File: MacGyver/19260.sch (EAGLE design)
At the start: 127 parts, among them J1 PST1,0/2-3,5, J10 RJ45J, J13 S04B, J2 PPPC101LFBN, J3 PPPC101LFBN, J4 PPPC101LFBN, J7 Pi Zero, J8 PST1,0/3-3,5, J9 RJ45J, Q1 IRFR5305, Q10 K38, Q11 K38, Q2 K1N, Q201 K1N, Q202 K1N, Q203 K1N, Q3 IRFR5305, Q4 P65, Q5 K3N, Q6 K1N, Q7 K3N, Q8 P65, Q9 K38, U1 1087, U2 1087, U201 74LVC07A, U202 74LVC07A, U203 THVD1500, U204 THVD1500, U205 THVD1500, U206 ATMEGA328PB-AU, U3 I50115, U4 I50115, U5 AVR128DA28-I/SP, Y201 12MHz

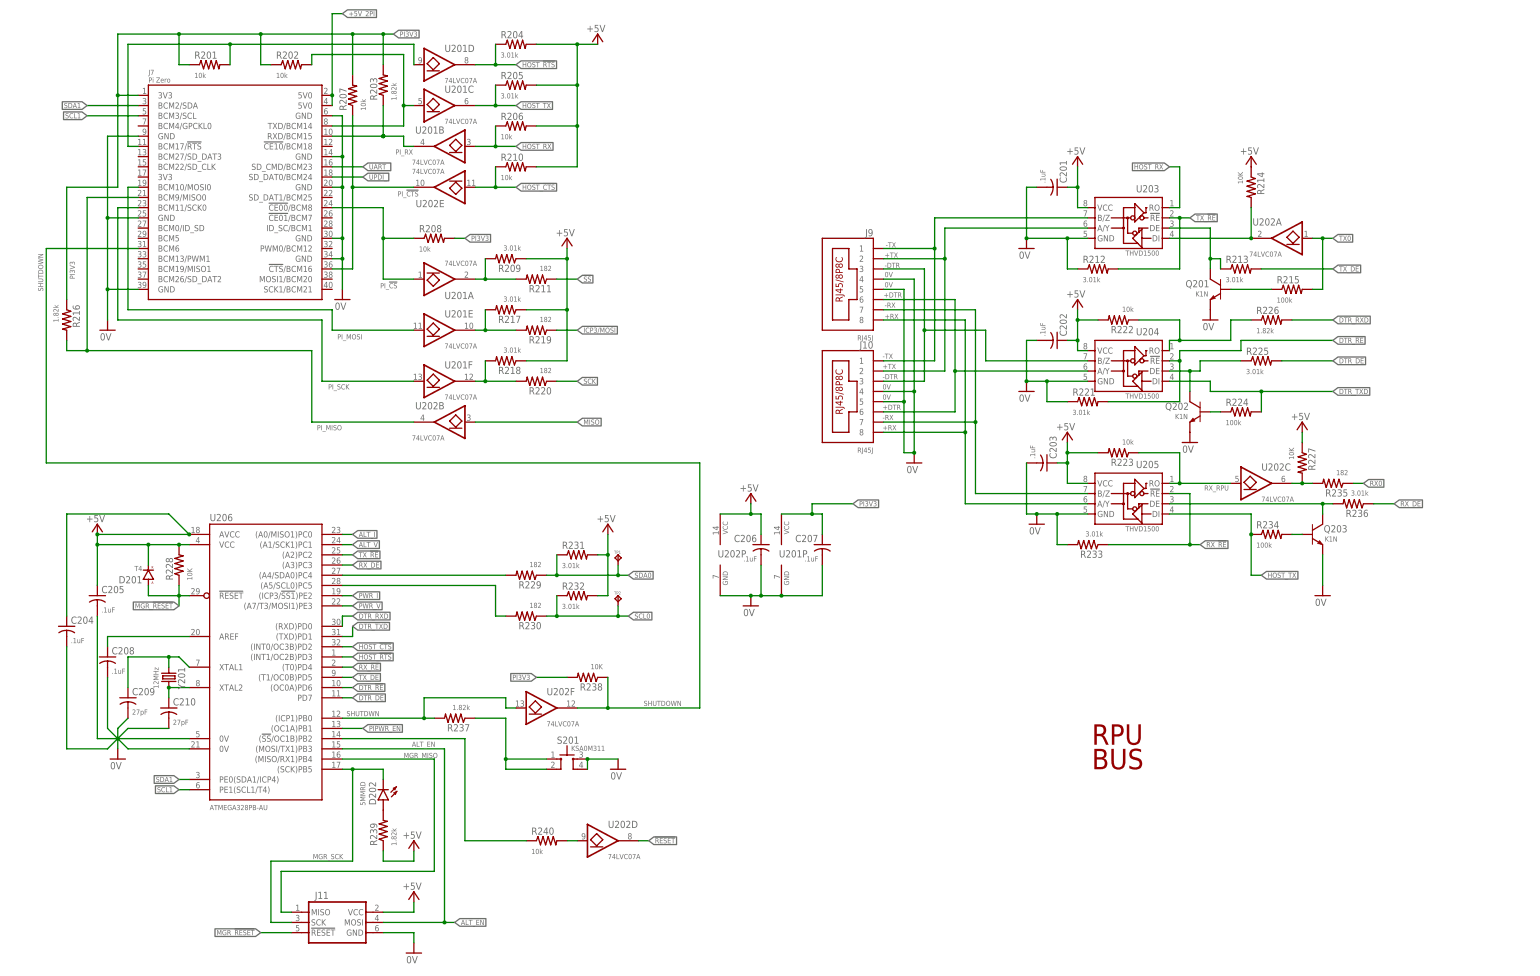
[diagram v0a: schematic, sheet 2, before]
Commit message: MacGyger: manager will be avr-db, remove spi
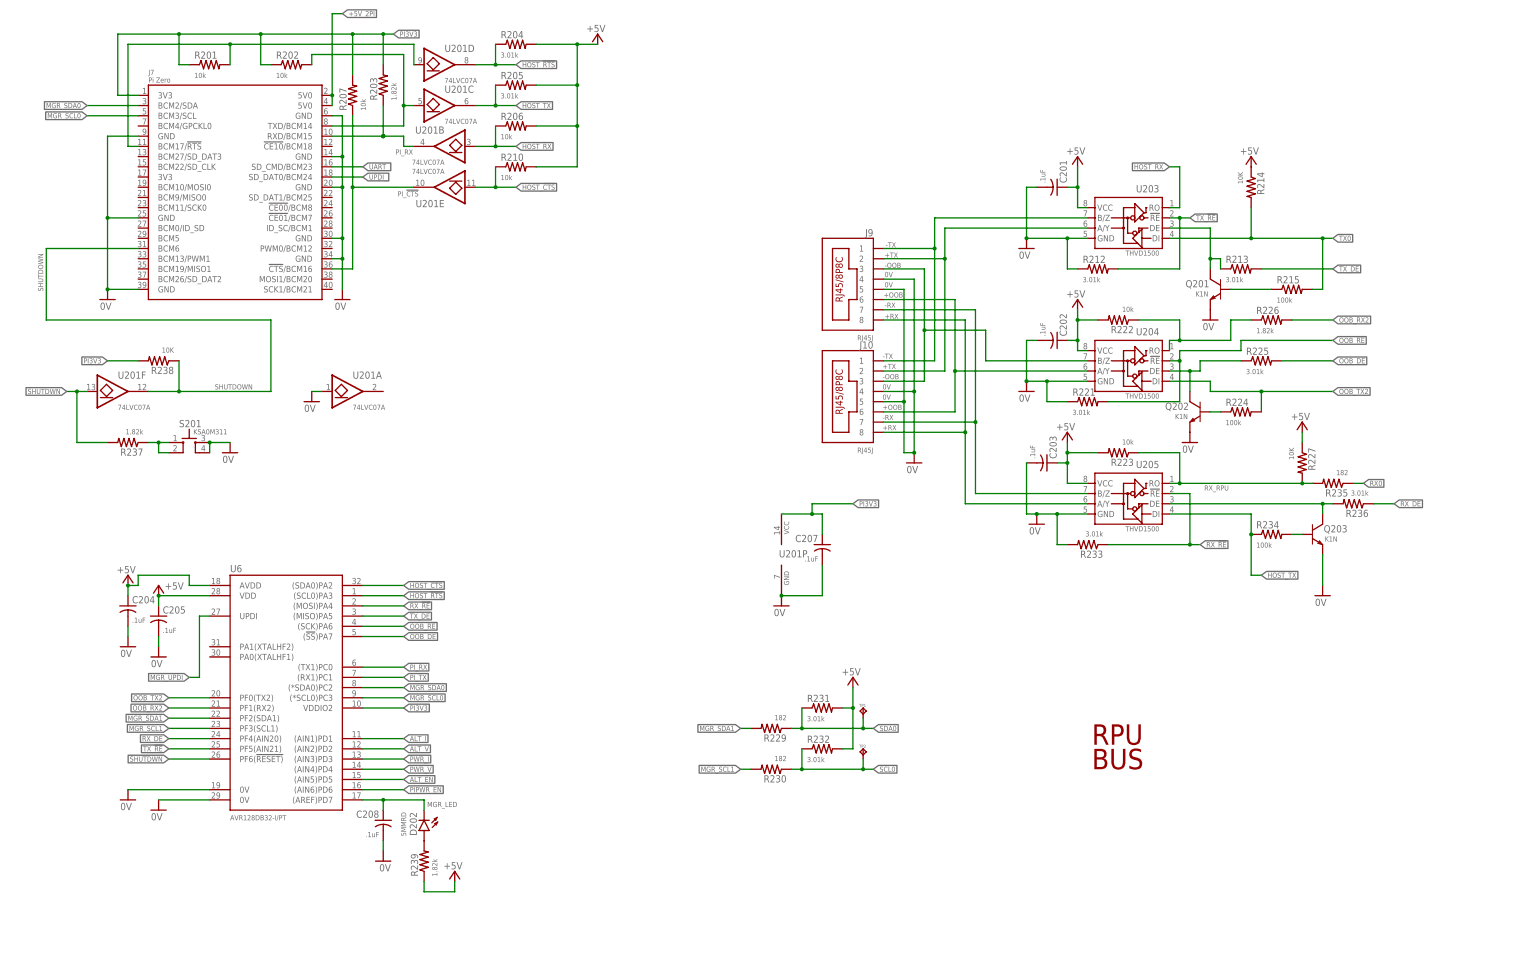
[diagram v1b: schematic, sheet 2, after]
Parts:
- removed C206: .1uF, C-C:CC0603A
- removed C209, C210: 27pF, C-C:CC0603A
- removed D201: T4, D-GP:DSOD123
- removed J11: (no value), U-AVR:ISP-SPIPTH
- removed R208, R240: 10k, R-C:R0805
- removed R209, R217, R218: 3.01k, R-C:R0805
- removed R211, R219, R220: 182, R-C:R0805
- removed R216: 1.82k, R-C:R0805
- removed R228: 10K, R-C:R0805
- removed U202: 74LVC07A, U-7400:7407D
- removed U206: ATMEGA328PB-AU, U-AVR:ATMEGA328PB-AU
- removed Y201: 12MHz, Y-XTL:CSM-3X
- added U6: AVR128DB32-I/PT, U-AVR:AVR128DB32
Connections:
- net +DTR renamed +OOB
- net -DTR renamed -OOB
- removed net !RESET!: U202D.O
- removed net DTR_!RE: R221.2, U204.!RE, U206.(OC0A)PD6
- removed net DTR_DE: R225.2, U206.PD7
- removed net DTR_RXD: R226.2, U206.(RXD)PD0
- removed net DTR_TXD: R224.2, U204.DI, U206.(TXD)PD1
- removed net ICP3/MOSI: R219.1
- removed net MGR_!RESET: D201.A, J11.!RESET, R228.1, U206.!RESET
- removed net MGR_!SS!: R240.1, U206.(!SS!/OC1B)PB2
- removed net MGR_AREF: C208.1, U206.AREF
- removed net MGR_MISO: J11.MISO, U206.(MISO/RX1)PB4
- removed net MGR_SCK: D202.K, J11.SCK, U206.(SCK)PB5
- removed net N$78: R227.2, R235.2, U202C.O
- removed net N$88: R240.2, U202D.I
- removed net N$91: R218.2, R220.2, U201F.O
- removed net N$92: R217.2, R219.2, U201E.O
- removed net N$94: R229.2, U206.(A4/SDA0)PC4
- removed net N$95: R230.2, U206.(A5/SCL0)PC5
- removed net N$96: R209.2, R211.2, U201A.O
- removed net PI_!CS: J7.!CE00!/BCM8, R208.1, U201A.I
- removed net PI_MISO: J7.BCM9/MISO0, R216.2, U202B.O
- removed net PI_MOSI: J7.BCM10/MOSI0, U201E.I
- removed net PI_SCK: J7.BCM11/SCK0, U201F.I
- removed net SCL1: J7.BCM3/SCL, U206.PE1(SCL1/T4)
- removed net SDA1: J7.BCM2/SDA, U206.PE0(SDA1/ICP4)
- removed net TX_RPU: R214.2, U202A.O, U203.DI
- removed net XTAL1: C209.1, U206.XTAL1, Y201.1
- removed net XTAL2: C210.1, U206.XTAL2, Y201.2
- new net MGR_LED: C208.1, D202.K, U6.(AREF)PD7
- new net MGR_SCL0: J7.BCM3/SCL, U6.(*SCL0)PC3
- new net MGR_SCL1: R230.2, U6.PF3(SCL1)
- new net MGR_SDA0: J7.BCM2/SDA, U6.(*SDA0)PC2
- new net MGR_SDA1: R229.2, U6.PF2(SDA1)
- new net MGR_UPDI: U6.UPDI
- new net OOB_!RE: R221.2, U204.!RE, U6.(SCK)PA6
- new net OOB_DE: R225.2, U6.(!SS!)PA7
- new net OOB_RX2: R226.2, U6.PF1(RX2)
- new net OOB_TX2: R224.2, U204.DI, U6.PF0(TX2)
- new net PI_TX: U6.(RX1)PC1
- net !SS: no longer R211.1
- net +5V: now also U6.AVDD, U6.VDD; no longer C206.1, D201.K, J11.VCC, R209.1, R217.1, R218.1, R228.2, U202P.VCC, U206.AVCC, U206.VCC@0
- net 0V: now also U201A.I, U6.0V@0, U6.0V@1; no longer C206.2, C209.2, C210.2, J11.GND, U202P.GND, U206.0V@0, U206.0V@1
- net ALT_EN: now also U6.(AIN5)PD5; no longer J11.MOSI, U206.(MOSI/TX1)PB3
- net ALT_I: now also U6.(AIN1)PD1; no longer U206.(A0/MISO1)PC0
- net ALT_V: now also U6.(AIN2)PD2; no longer U206.(A1/SCK1)PC1
- net HOST_!CTS: now also U201E.I, U6.(SDA0)PA2; no longer U202E.I, U206.(INT0/OC3B)PD2
- net HOST_!RTS: now also U6.(SCL0)PA3; no longer U206.(INT1/OC2B)PD3
- net MISO: no longer U202B.I
- net PI3V3: now also U6.VDDIO2; no longer R208.2, R216.1
- net PIPWR_EN: now also U6.(AIN6)PD6; no longer U206.(OC1A)PB1
- net PI_!CTS: now also U201E.O; no longer U202E.O
- net PI_RX: now also U6.(TX1)PC0
- net PWR_I: now also U6.(AIN3)PD3; no longer U206.(ICP3/!SS1!)PE2
- net PWR_V: now also U6.(AIN4)PD4; no longer U206.(A7/T3/MOSI1)PE3
- net RX_!RE: now also U6.(MOSI)PA4; no longer U206.(T0)PD4
- net RX_DE: now also U6.PF4(AIN20); no longer U206.(A3)PC3
- net RX_RPU: now also R227.2, R235.2; no longer U202C.I
- net SCK: no longer R220.1
- net SHUTDOWN: now also U201F.O; no longer U202F.O
- net SHUTDWN: now also U201F.I, U6.PF6(!RESET); no longer U202F.I, U206.(ICP1)PB0
- net TX0: now also R214.2, U203.DI; no longer U202A.I
- net TX_!RE: now also U6.PF5(AIN21); no longer U206.(A2)PC2
- net TX_DE: now also U6.(MISO)PA5; no longer U206.(T1/OC0B)PD5
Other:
- note added: "1"
- note added: "15"
- note added: "17"
- note added: "2"
- note added: "25"
- note added: "32"
- note added: "BUS MANAGER NEEDS TO DRIVE OOB_DE BUT A HIGH OOB_TX OVERIDES"
- note added: "I2C to APP"
- note added: "IF AREF NEEDS BYPASS"
- note added: "MVIO"
- note added: "OOB"
- note added: "OUT OF BAND"
- note added: "SMBus to Pi"
- note added: "debug"
- note removed: "BUS MANAGER NEEDS TO DRIVE DTR_DE BUT A HIGH DTR_TXD OVERIDES"
- note removed: "CNTL RESET"
- note removed: "CRYSTAL: ECS-120-20-3X-TR 12MHZ +/- 30PPM STABILITY AND TOLERANCE CRYSTAL CAPACITORS: 20PF = 6.5PF + (27PF*27PF)/(27PF+27PF)"
- note removed: "DTR"
- note removed: "MGR ICSP"
- note removed: "REMOVE ALTERNAT POWER BEFOR ISP PROGRAMING"
- moved on the sheet: C204, C205, C208, D202, R229, R230, R231, R232, R237, R238, R239, S201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

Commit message: MacGyver: remove rts/cts since no bootloader
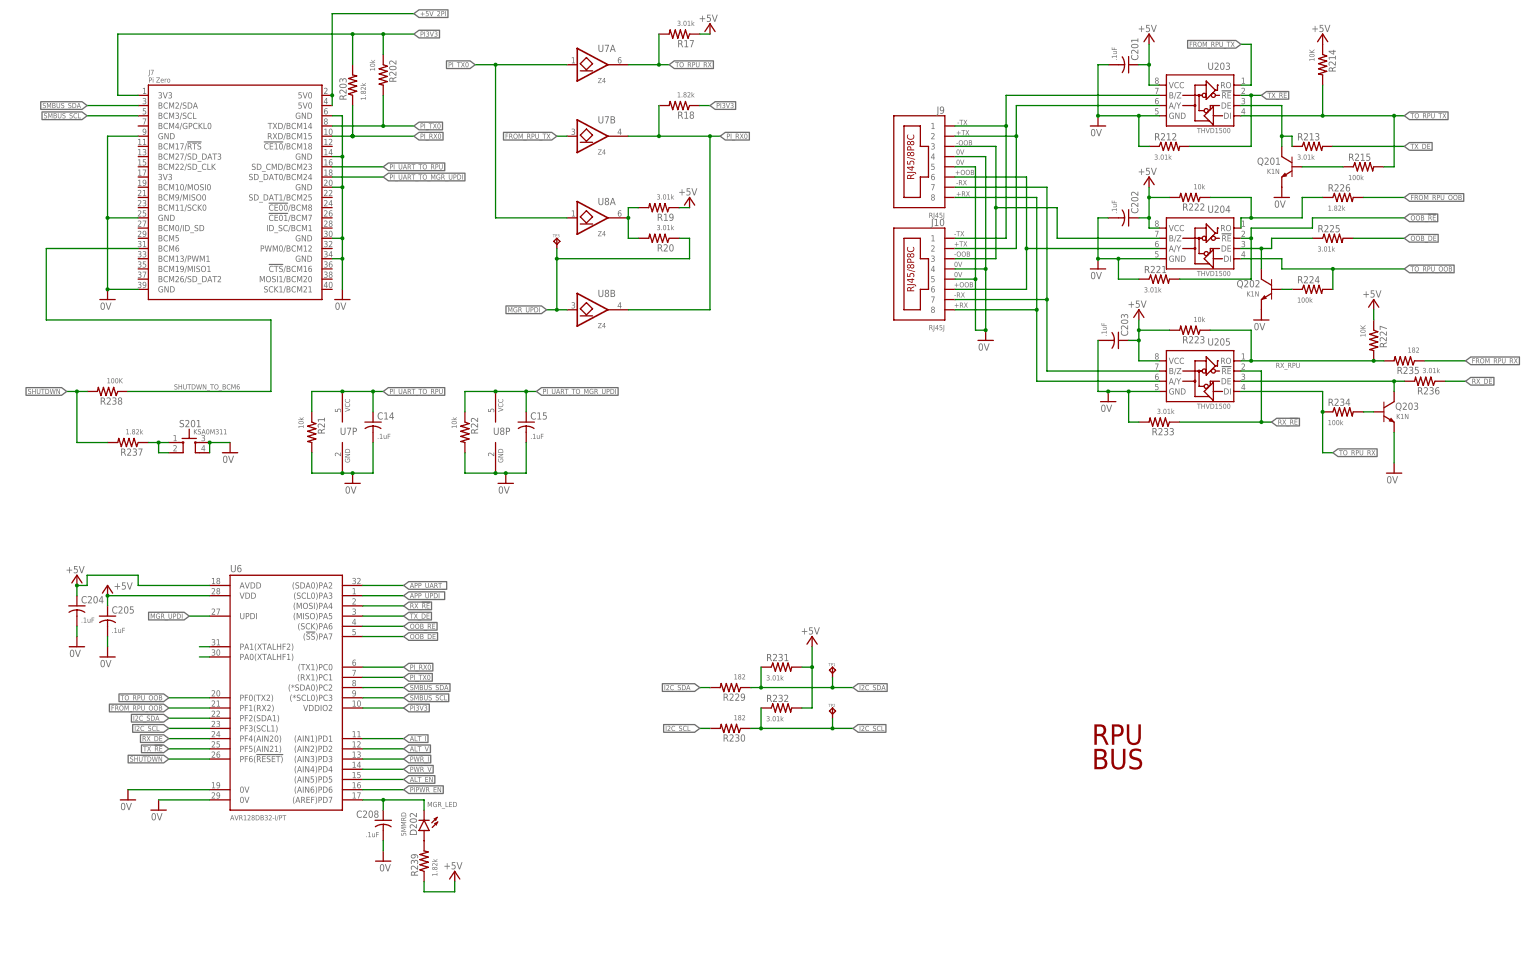
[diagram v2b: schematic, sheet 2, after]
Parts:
- removed C207: .1uF, C-C:CC0603A
- removed R201, R206, R207, R210: 10k, R-C:R0805
- removed R204, R205: 3.01k, R-C:R0805
- removed U201: 74LVC07A, U-7400:7407D
- added C14, C15, C16, C17: .1uF, C-C:CC0603A
- added R17, R19, R20, R23, R24, R25, R26: 3.01k, R-C:R0805
- added R18: 1.82k, R-C:R0805
- added R21, R22, R27, R28: 10k, R-C:R0805
- added TP3: TPPAD1-08, J-TP:TPPAD1-08
- added U10, U7, U8, U9: Z4, U-7400:2G07SOT26
- R238: value 10K -> 100K
- R3: value 0.018 -> 0.010
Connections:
- net MGR_SCL0 renamed SMBUS_SCL
- net MGR_SCL1 renamed I2C_SCL_
- net MGR_SDA0 renamed SMBUS_SDA
- net MGR_SDA1 renamed I2C_SDA_
- net OOB_RX2 renamed FROM_RPU_OOB
- net OOB_TX2 renamed TO_RPU_OOB
- net SCL0 renamed I2C_SCL
- net SDA0 renamed I2C_SDA
- removed net HOST_!CTS: R210.1, U201E.I, U6.(SDA0)PA2
- removed net HOST_!RTS: R204.1, U201D.O, U6.(SCL0)PA3
- removed net HOST_RX: R206.1, U201B.I, U203.RO
- removed net HOST_TX: R205.1, R234.1, U201C.O, U205.DI
- removed net N$89: J7.TXD/BCM14, R202.2, U201C.I
- removed net N$90: J7.BCM17/!RTS!, R201.2, U201D.I
- removed net PI_!CTS: J7.!CTS!/BCM16, R207.1, U201E.O
- removed net PI_RX: J7.RXD/BCM15, R203.1, U201B.O, U6.(TX1)PC0
- removed net PI_TX: U6.(RX1)PC1
- removed net RX0: J4.7, R235.1, U5.(RX0)PA1
- removed net SHUTDOWN: J7.BCM6, R238.1, U201F.O
- removed net TX0: J4.6, R214.2, R215.2, U203.DI, U5.(EXTCLK/TX0)PA0
- removed net UART_: J7.SD_CMD/BCM23
- removed net UPDI_: J7.SD_DAT0/BCM24
- new net APP_RX0: J4.7, R23.2, U5.(RX0)PA1, U9A.O
- new net APP_TX0: J4.6, U5.(EXTCLK/TX0)PA0, U9B.I
- new net APP_UART_: C16.1, R27.1, U6.(SDA0)PA2, U9P.VCC
- new net APP_UPDI_: C17.1, R28.1, U10P.VCC, U6.(SCL0)PA3
- new net FROM_RPU_RX: R235.1, U10A.I, U9A.I
- new net FROM_RPU_TX: U203.RO, U7B.I
- new net N$1: R19.2, R20.2, U8A.O
- new net N$11: U6.PA0(XTALHF1)
- new net N$3: R25.2, R26.2, U10A.O
- new net N$9: U6.PA1(XTALHF2)
- new net PI_RX0: J7.RXD/BCM15, R18.2, R203.1, U6.(TX1)PC0, U7B.O, U8B.O
- new net PI_TX0: J7.TXD/BCM14, R202.2, U6.(RX1)PC1, U7A.I, U8A.I
- new net PI_UART_TO_MGR_UPDI: C15.1, J7.SD_DAT0/BCM24, R22.1, U8P.VCC
- new net PI_UART_TO_RPU: C14.1, J7.SD_CMD/BCM23, R21.1, U7P.VCC
- new net SHUTDWN_TO_BCM6: J7.BCM6, R238.1
- new net TO_RPU_RX: R17.2, R234.1, U205.DI, U7A.O
- new net TO_RPU_TX: R214.2, R215.2, R24.2, U10B.O, U203.DI, U9B.O
- net +5V: now also R17.1, R19.1, R23.1, R24.1, R25.1; no longer R204.2, R205.2, R206.2, R210.2
- net 0V: now also C14.2, C15.2, C16.2, C17.2, R21.2, R22.2, R27.2, R28.2, U10P.GND, U7P.GND, U8P.GND, U9P.GND; no longer C207.2, U201A.I, U201P.GND
- net MGR_UPDI: now also R20.1, TP3.TP, U8B.I
- net PI3V3: now also R18.1; no longer C207.1, R201.1, R207.2, R238.2, U201P.VCC
- net SHUTDWN: now also R238.2; no longer U201F.I
- net UPDI-APP: now also R26.1, U10B.I
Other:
- note added: "DRIVE SIDE DOES NOT NEED PULL-UP"
- note added: "ENABLE NORMAL FULL DUPLEX SERIAL FROM RPU TO APPLICATION ON ITS UART0"
- note added: "ENABLE NORMAL FULL DUPLEX SERIAL TO RPU"
- note added: "ENABLE UNIFIED PROGRAMING ... INTERFACE FROM PI TO MANAGER"
- note added: "ENABLE UNIFIED PROGRAMING ... INTERFACE FROM RPU TO APPLICATION"
- note added: "EXAMPLES: https://github.com/epccs/MacGyver/"
- note added: "MGR UPDI TO R-PI"
- note added: "PASSIVE SIDE NEEDS A PULL-UP"
- note added: "RPU TX/RX TO R-PI"
- note added: "UART0_SYS"
- note added: "UART1"
- note added: "UART2"
- note added: "UART_0 TO APPLICATION"
- note added: "https://github.com/mraardvark/pyupdi"
- note removed: "1"
- note removed: "32"
- note removed: "EXAMPLES: https://github.com/epccs/Gravimetric/"
- note removed: "IF THE 3V3PI IS OFF THE 74LVC07 OPEN DRAIN IS HI-Z (IOFF)."
- note removed: "UART_0_SYS"
- note removed: "UART_1"
- note removed: "UART_2"
- moved on the sheet: C12, C13, C201, C202, C203, C204, C205, C4, C5, J10, J13, J9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
